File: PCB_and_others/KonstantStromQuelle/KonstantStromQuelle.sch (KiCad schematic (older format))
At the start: 10 parts

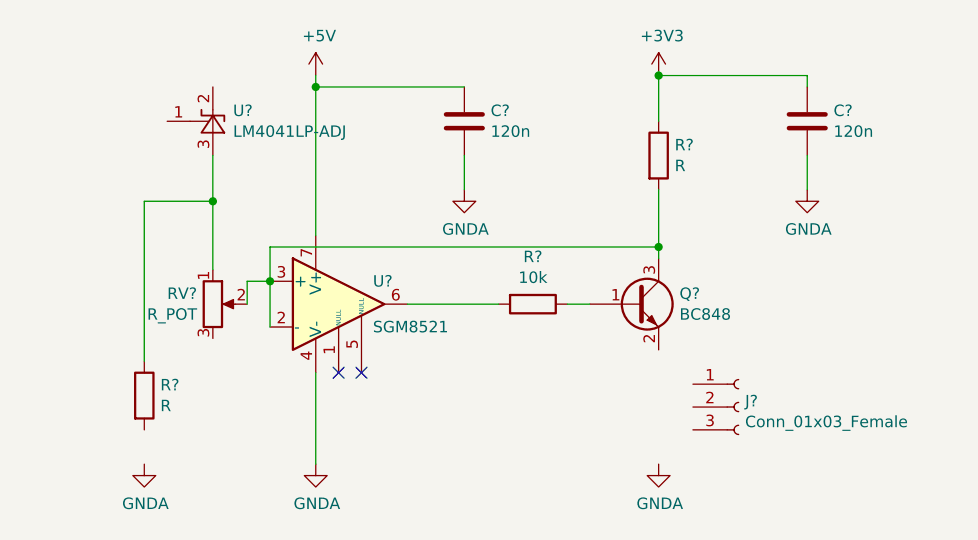
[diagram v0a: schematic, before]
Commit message: Beeper Impl.
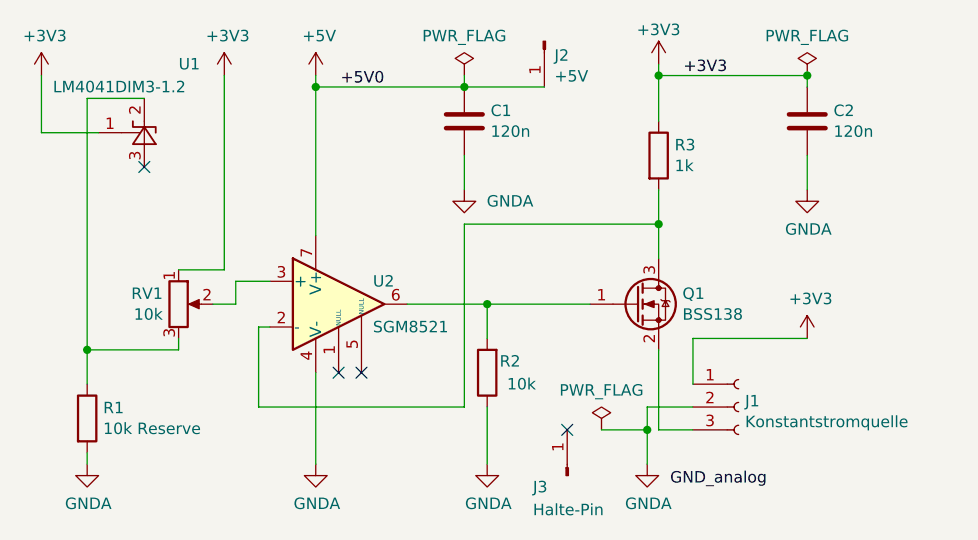
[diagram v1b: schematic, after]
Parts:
- removed Q?: BC848, Package_TO_SOT_SMD:SOT-23, symbol Transistor_BJT:BC848
- added J2: +5V, Connector_Pin:Pin_D0.9mm_L10.0mm_W2.4mm_FlatFork, symbol Connector:Conn_01x01_Male
- added J3: Halte-Pin, Connector_Pin:Pin_D0.9mm_L10.0mm_W2.4mm_FlatFork, symbol Connector:Conn_01x01_Male
- added Q1: BSS138, Package_TO_SOT_SMD:SOT-23, symbol Transistor_FET:BSS138
- J1: renamed from J?; value Conn_01x03_Female -> Konstantstromquelle; footprint (none) -> Package_TO_SOT_THT:TO-92L_Inline_Wide
- R1: renamed from R?; value R -> 10k Reserve; footprint (none) -> Resistor_SMD:R_1206_3216Metric_Pad1.42x1.75mm_HandSolder
- R3: renamed from R?; value R -> 1k; footprint (none) -> Resistor_SMD:R_1206_3216Metric_Pad1.42x1.75mm_HandSolder
- RV1: renamed from RV?; value R_POT -> 10k; footprint (none) -> Potentiometer_THT:Potentiometer_Bourns_3296W_Vertical
- U1: renamed from U?; value LM4041LP-ADJ -> LM4041DIM3-1.2; footprint Package_TO_SOT_THT:TO-92_Inline -> Package_TO_SOT_SMD:SOT-23
- gave numbers to parts that had none: 4
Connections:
- net +3V3: now also J1.1 (Pin_1), RV1.1, U1.1 (FB)
- net +5V: now also J2.1 (Pin_1)
- net GNDA: now also J1.2 (Pin_2), R1.2, R2.1
- net at R3.2, U2.2 (-): now also Q1.3 (D); no longer RV1.2, U2.3 (+)
- net at R2.2, U2.6: now also Q1.1 (G)
- net at RV1.3: now also R1.1, U1.2 (K)
- net at J1.3 (Pin_3): now also Q1.2 (S)
- new net: RV1.2, U2.3 (+)
- now unconnected: U1.3 (A)
- no-connect marks 2 -> 4
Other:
- moved on the sheet: R1, R2, RV1, U1
